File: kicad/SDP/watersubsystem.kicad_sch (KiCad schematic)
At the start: 14 parts, among them J11 Conn_01x02, J14 Conn_01x02, J15 Conn_01x07, J16 Conn_01x07, J17 Conn_01x03, J18 Conn_01x03, Q1 IRLZ44N, Q2 IRLZ44N

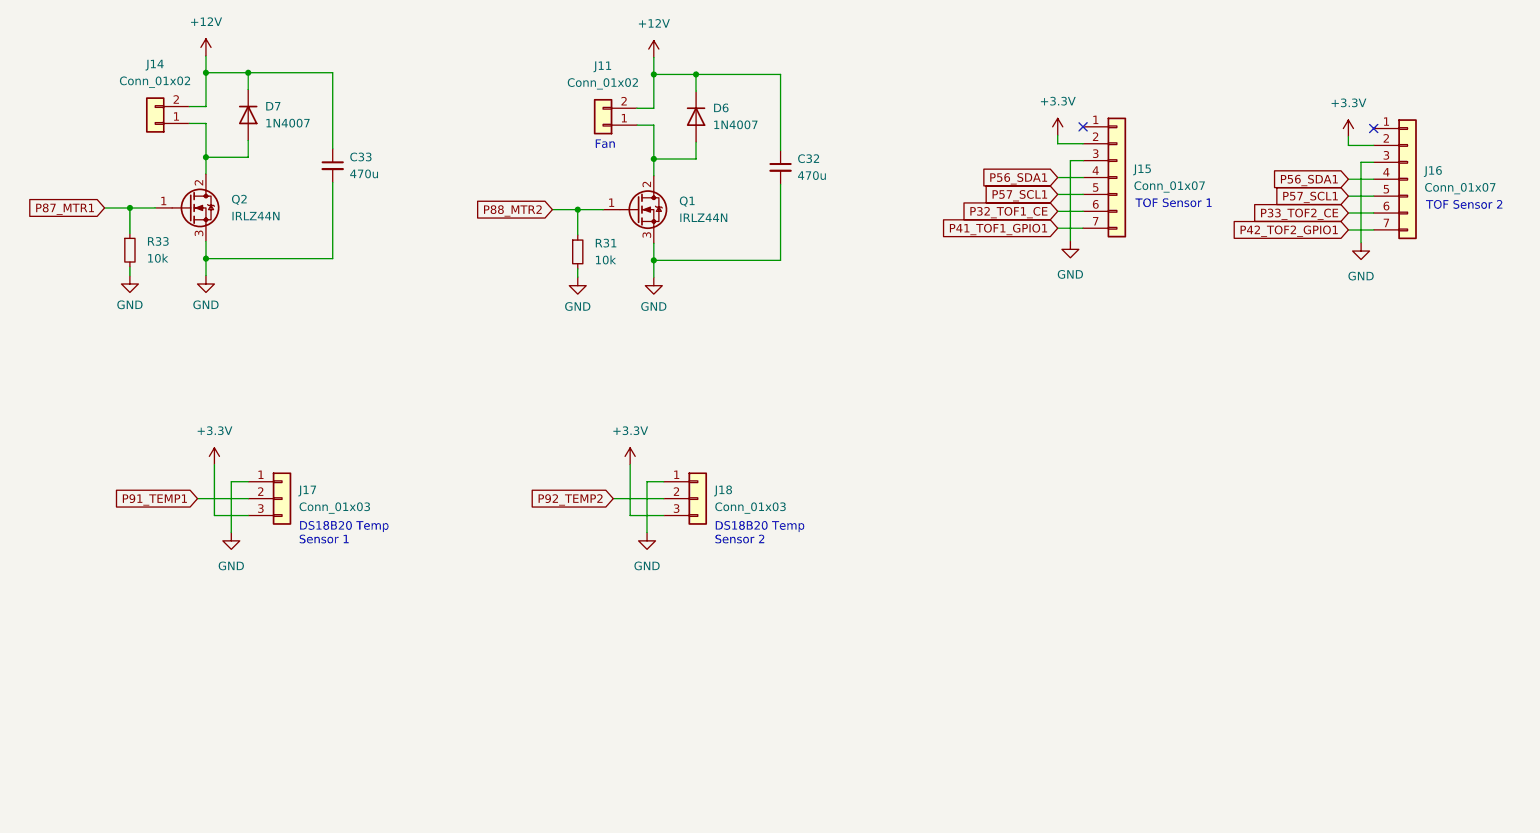
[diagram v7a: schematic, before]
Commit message: Assigned footprints, added limit switches, rearranged schematics
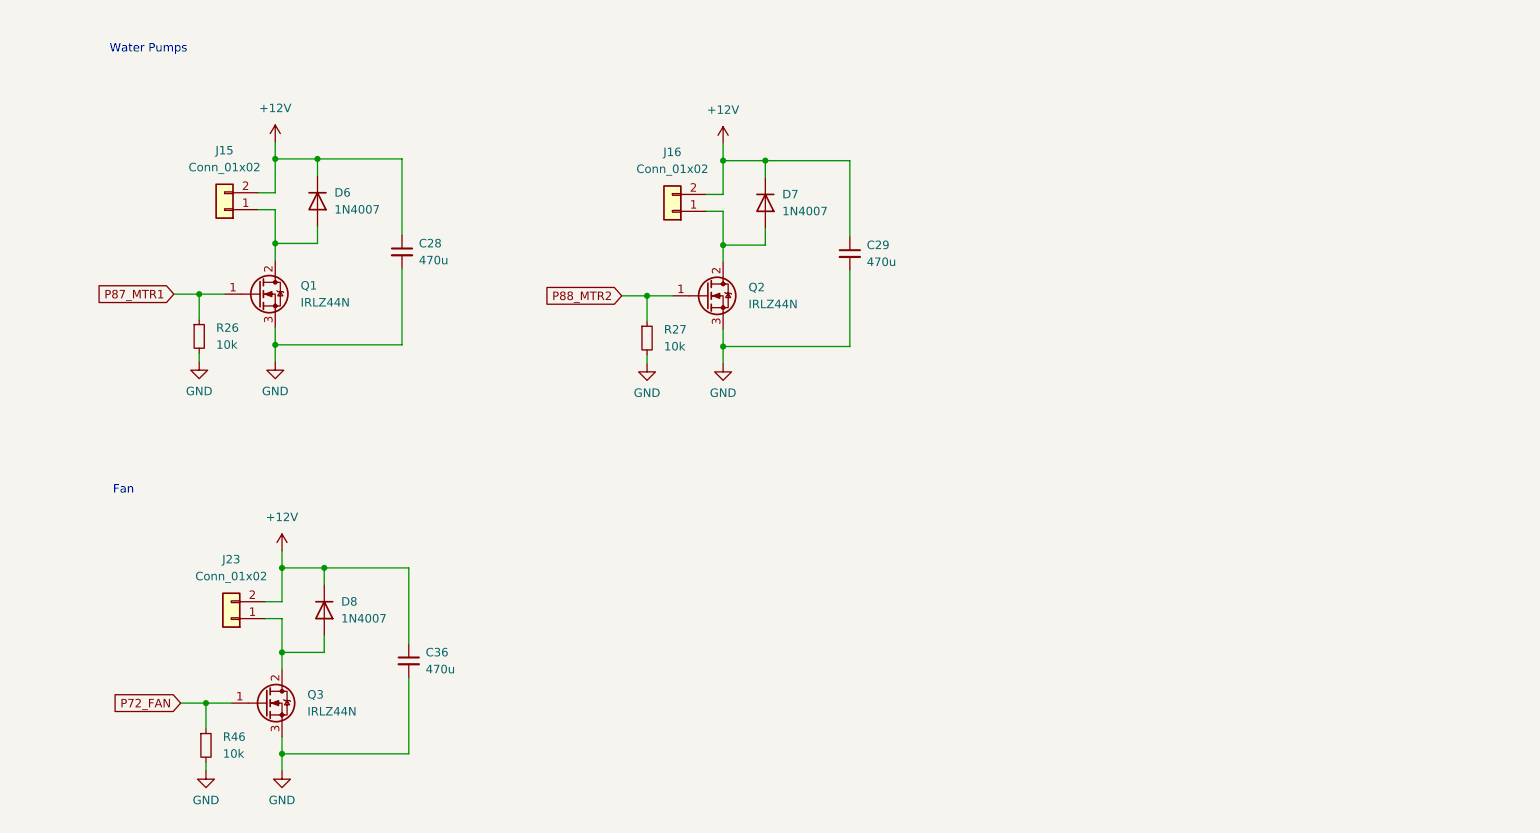
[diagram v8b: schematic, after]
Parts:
- removed C32, C33: 470u, symbol Device:C_Small
- removed J11, J14: Conn_01x02, symbol Connector_Generic:Conn_01x02
- removed J15, J16: Conn_01x07, symbol Connector_Generic:Conn_01x07
- removed J17, J18: Conn_01x03, symbol Connector_Generic:Conn_01x03
- removed R31, R33: 10k, Resistor_SMD:R_0805_2012Metric, symbol Device:R_Small
- added C28, C29, C36: 470u, symbol Device:C_Small
- added D8: 1N4007, Diode_THT:D_DO-41_SOD81_P10.16mm_Horizontal, symbol Diode:1N4007
- added J15, J16, J23: Conn_01x02, Connector_PinSocket_2.54mm:PinSocket_1x02_P2.54mm_Vertical, symbol Connector_Generic:Conn_01x02
- added Q3: IRLZ44N, Package_TO_SOT_THT:TO-220-3_Vertical, symbol Transistor_FET:IRLZ44N
- added R26, R27, R46: 10k, Resistor_SMD:R_0805_2012Metric, symbol Device:R_Small
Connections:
- net +12V: now also C28.1, C29.1, C36.1, D8.1 (K), J15.2 (Pin_2), J16.2 (Pin_2), J23.2 (Pin_2)
- net GND: now also C28.2, C29.2, C36.2, Q3.3 (S), R26.2, R27.2, R46.2
- net P87_MTR1: now also Q1.1 (G), R26.1; no longer Q2.1 (G)
- net P88_MTR2: now also Q2.1 (G), R27.1; no longer Q1.1 (G)
- net at D6.2 (A), Q1.2 (D): now also J15.1 (Pin_1)
- net at D7.2 (A), Q2.2 (D): now also J16.1 (Pin_1)
- new net: D8.2 (A), J23.1 (Pin_1), Q3.2 (D)
- new net P72_FAN: Q3.1 (G), R46.1
- no-connect marks 2 -> 0
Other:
- note added: "Water Pumps"
- note removed: "DS18B20 Temp Sensor 1"
- note removed: "DS18B20 Temp Sensor 2"
- note removed: "TOF Sensor 1"
- note removed: "TOF Sensor 2"
